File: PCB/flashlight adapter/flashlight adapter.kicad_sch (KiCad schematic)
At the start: 26 parts, among them J1 USB4105-GF-A, Q1 Q_NMOS_Depletion, Q2 Q_NMOS_Depletion, U1 MIC2295YD5-TR, U3 BQ24074RGT, U4 DW01A

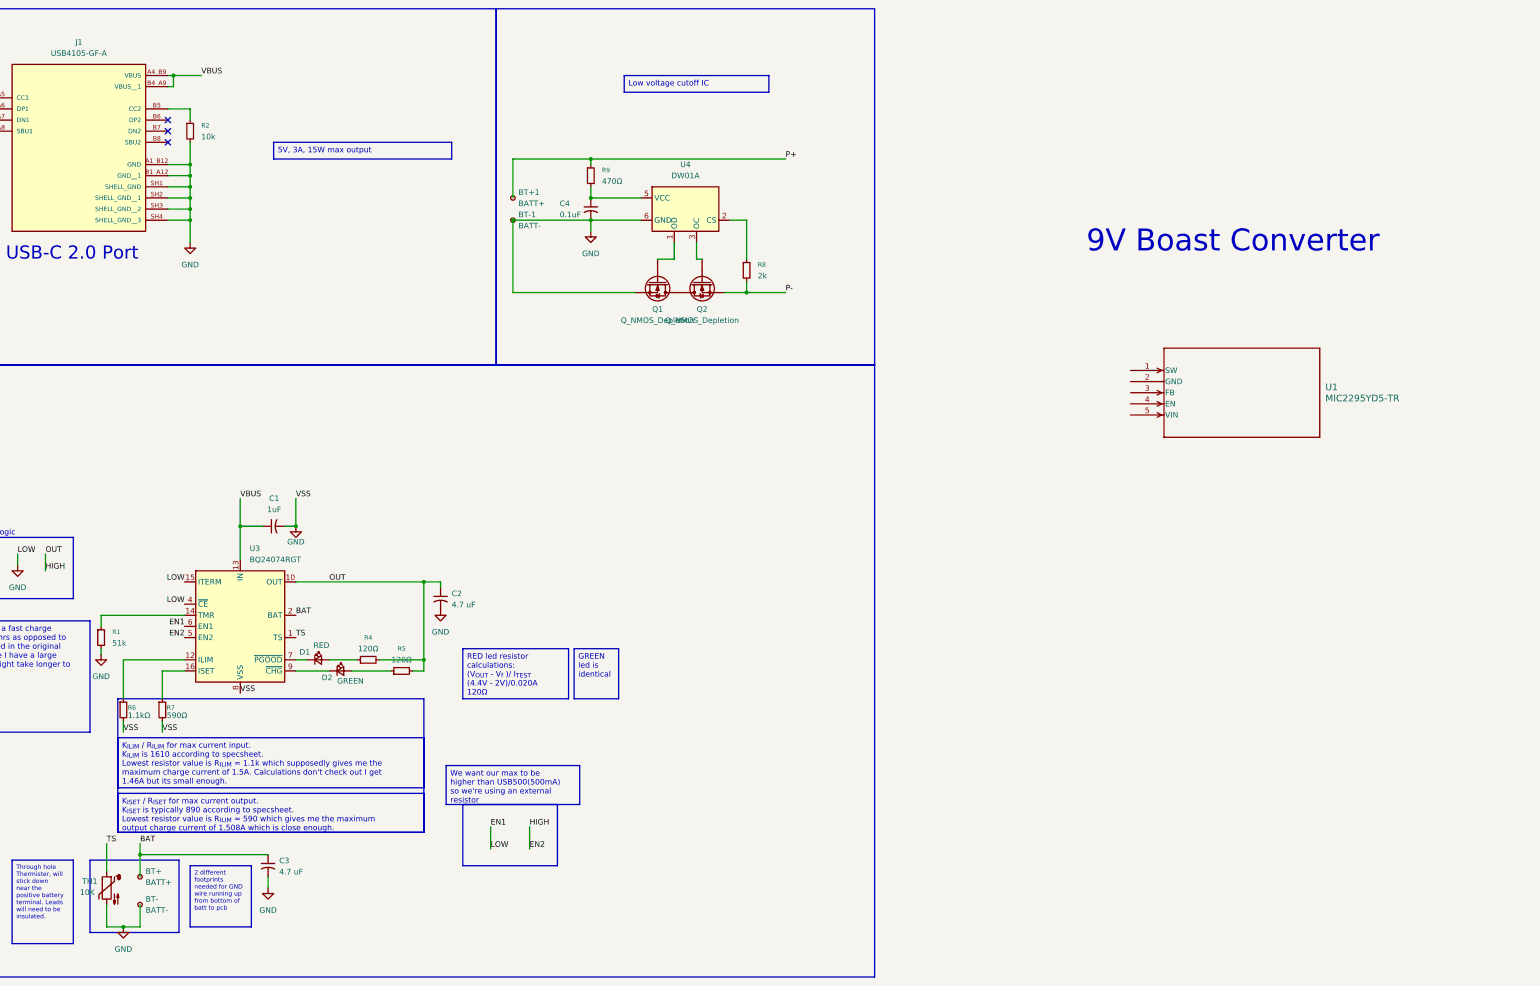
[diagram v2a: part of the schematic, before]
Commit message: almost completed boast converter, waiting on inductor resistor feedback
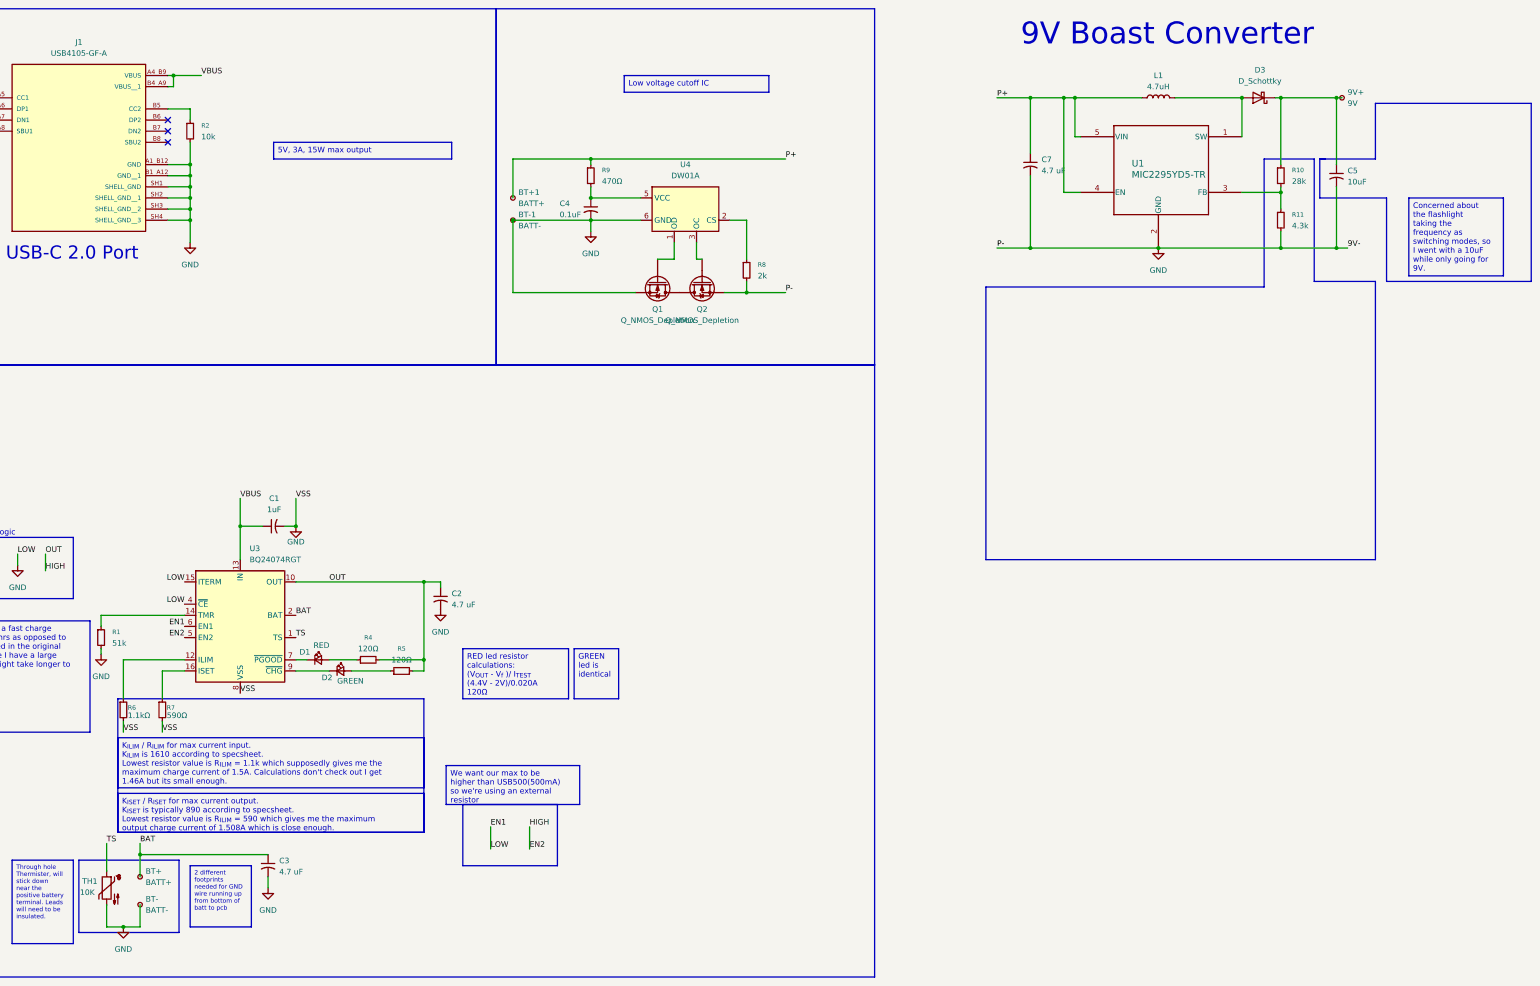
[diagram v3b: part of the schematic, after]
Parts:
- added 9V+: 9V, symbol Connector:TestPoint_Small
- added C5: 10uF, Capacitor_SMD:C_0805_2012Metric_Pad1.18x1.45mm_HandSolder, symbol Device:C_Small_US
- added C7: 4.7 uF, Capacitor_SMD:C_0603_1608Metric_Pad1.08x0.95mm_HandSolder, symbol Device:C_Small_US
- added D3: D_Schottky, Diode_SMD:D_SMA_Handsoldering, symbol Device:D_Schottky
- added L1: 4.7uH, Inductor_SMD:L_1008_2520Metric_Pad1.43x2.20mm_HandSolder, symbol Device:L
- added R10: 28k, Resistor_SMD:R_0603_1608Metric_Pad0.98x0.95mm_HandSolder, symbol Device:R_Small
- added R11: 4.3k, Resistor_SMD:R_0603_1608Metric_Pad0.98x0.95mm_HandSolder, symbol Device:R_Small
- U1: footprint Package_TO_SOT_SMD:TSOT-23-5_HandSoldering -> TSOT-23-5_D5_MCH
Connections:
- net P- is gone; now on net GND: Q2.S, R8.2
- net GND: now also U1.2 (GND), C5.2, C7.2, R11.2
- net P+: now also U1.4 (EN), U1.5 (VIN), C7.1, L1.1
- net at U1.1 (SW): now also D3.2 (A), L1.2
- net at U1.3 (FB): now also R10.2, R11.1
- new net: 9V+.1, C5.1, D3.1 (K), R10.1

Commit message: Pretty much finished schematic
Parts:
- removed BT+1: BATT+, symbol Connector:TestPoint_Small
- removed BT-1: BATT-, symbol Connector:TestPoint_Small
- 9V+1: renamed from 9V+; footprint (none) -> pads:4mm_by_4mm_pad
- BT+1: renamed from BT+; footprint (none) -> pads:4mm_by_4mm_pad
- BT-1: renamed from BT-; footprint (none) -> pads:3mm_by_4mm_pad
- J1: footprint USB4105-GF-A:GCT_USB4105-GF-A -> USB4105_GF_A:GCT_USB4105-GF-A
- Q1: footprint (none) -> DN2625K4:TO-252-3_MCH-L; symbol Device:Q_NMOS_Depletion -> Transistor_FET_Other:Q_NMOS_Depletion_GSD
- Q2: value Q_NMOS_Depletion -> Q_NMOS_Depletion_GSD; footprint (none) -> DN2625K4:TO-252-3_MCH-L; symbol Device:Q_NMOS_Depletion -> Transistor_FET_Other:Q_NMOS_Depletion_GSD
- U3: renamed from U1; footprint TSOT-23-5_D5_MCH -> Package_TO_SOT_SMD:TSOT-23-5_HandSoldering
- renumbered C3 to C1, C1 to C2, C2 to C3, C7 to C5, C5 to C6, R3 to R1, R1 to R2, R6 to R3, R7 to R4, R2 to R5, R4 to R6, R5 to R7, R9 to R8, R8 to R9, U3 to U1, U4 to U2
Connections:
- net P+ is gone; now on net BAT: C5.1, L1.1, R8.1, U3.4 (EN), U3.5 (VIN)
- net GND: now also Q1.2 (S), Q2.2 (S); no longer Q1.S, Q2.S
- net at U2.1 (OD): now also Q1.1 (G); no longer Q1.G
- net at U2.3 (OC): now also Q2.1 (G); no longer Q2.G
- new net: Q1.3 (D), Q2.3 (D)

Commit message: Intial layout complete with DRC, test pads to be added
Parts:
- removed Q1: Q_NMOS_Depletion, DN2625K4:TO-252-3_MCH-L, symbol Transistor_FET_Other:Q_NMOS_Depletion_GSD
- removed Q2: Q_NMOS_Depletion_GSD, DN2625K4:TO-252-3_MCH-L, symbol Transistor_FET_Other:Q_NMOS_Depletion_GSD
- added Q1: FS8205A, FS8205A:SOP65P640X120-8N, symbol FS8205A:FS8205A
- D3: footprint Diode_SMD:D_SMA_Handsoldering -> Diode_SMD:D_SOD-123F
- R9: value 2k -> 2kΩ
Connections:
- net GND: now also Q1.2, Q1.3; no longer C5.2, C6.2, R11.2, R9.2, U3.2 (GND)
- net at U2.1 (OD): now also Q1.4
- net at U2.3 (OC): now also Q1.5
- new net: Q1.1, Q1.8
- new net P-: C5.2, C6.2, Q1.6, Q1.7, R11.2, R9.2, U3.2 (GND)
- no-connect marks 6 -> 7

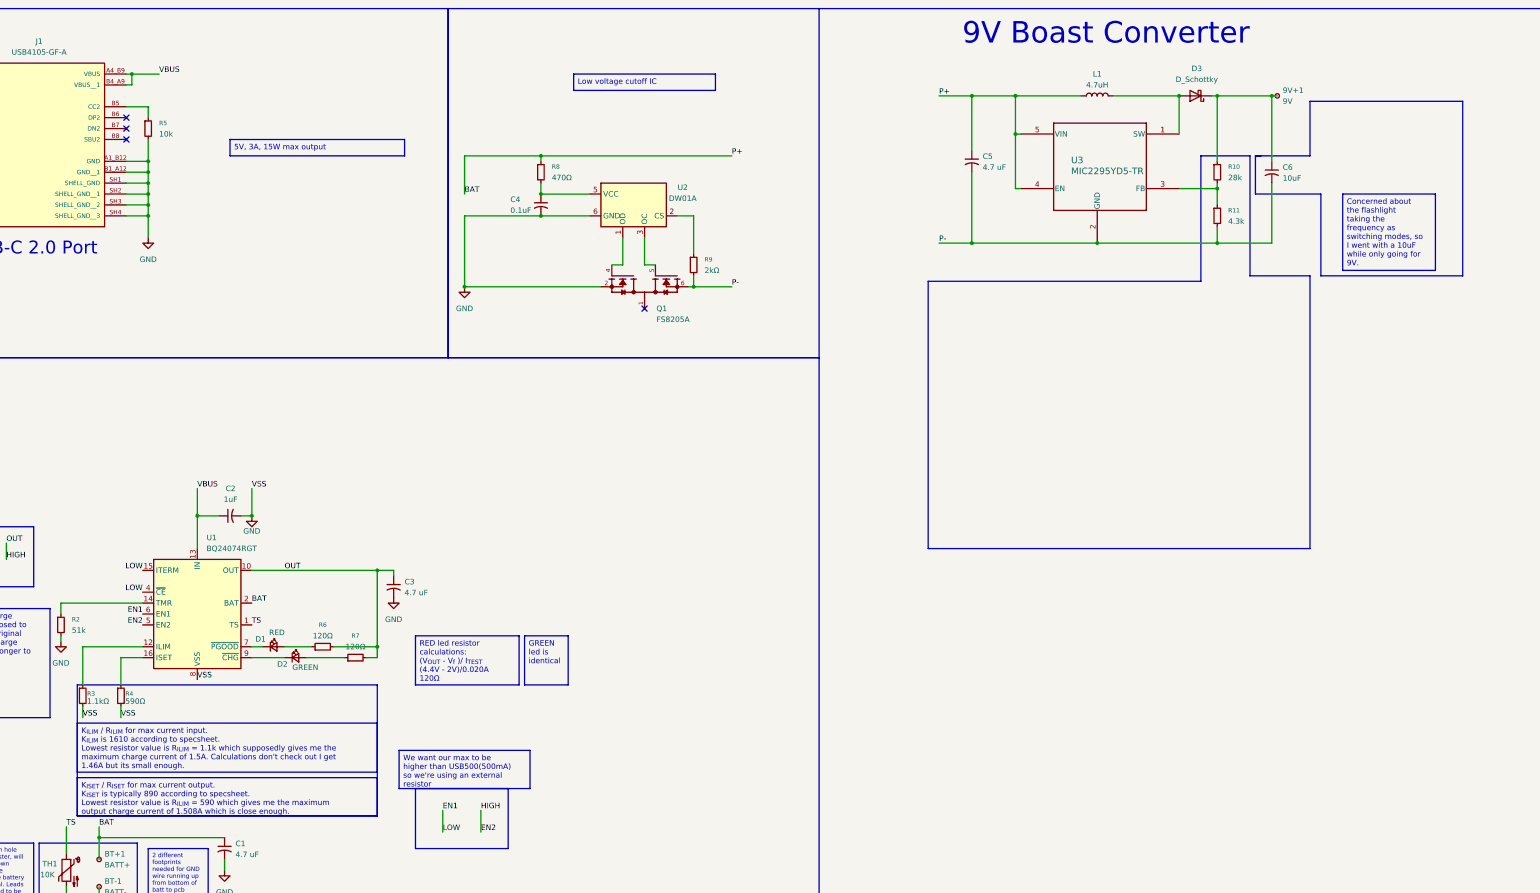
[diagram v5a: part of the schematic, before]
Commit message: Added Boost off when charging
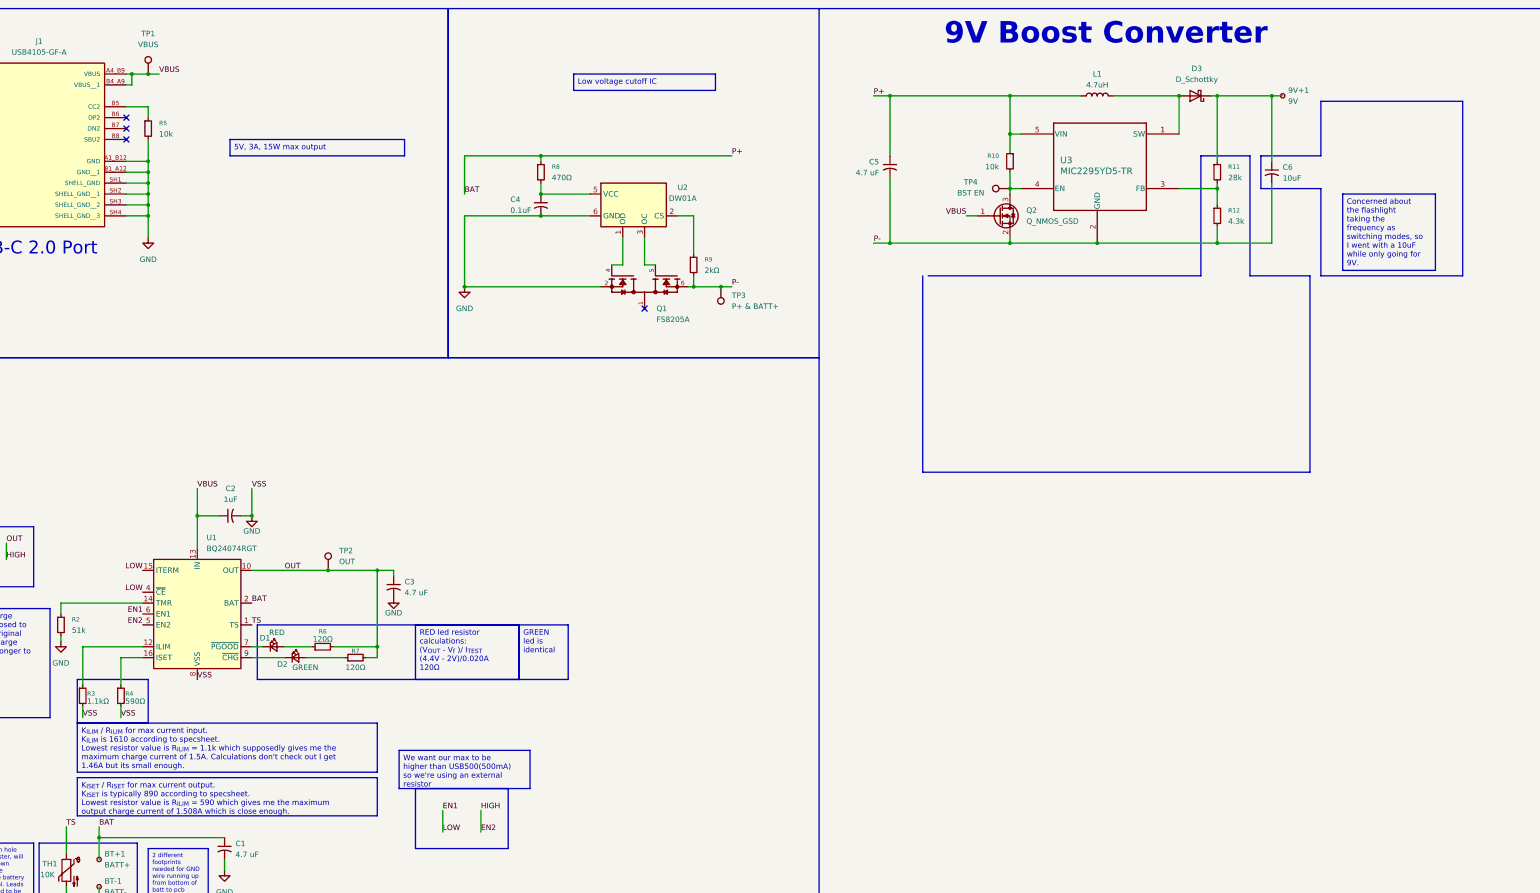
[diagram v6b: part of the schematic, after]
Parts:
- added Q2: Q_NMOS_GSD, Package_TO_SOT_SMD:SOT-23_Handsoldering, symbol Transistor_FET:Q_NMOS_GSD
- added R10: 10k, Resistor_SMD:R_0603_1608Metric_Pad0.98x0.95mm_HandSolder, symbol Device:R_Small
- added TP1: VBUS, TestPoint:TestPoint_Pad_D1.5mm, symbol Connector:TestPoint
- added TP2: OUT, TestPoint:TestPoint_Pad_D1.5mm, symbol Connector:TestPoint
- added TP3: P+ & BATT+, TestPoint:TestPoint_Pad_D1.5mm, symbol Connector:TestPoint
- added TP4: BST EN, TestPoint:TestPoint_Pad_D1.5mm, symbol Connector:TestPoint
- Q1: footprint FS8205A:SOP65P640X120-8N -> Package_TO_SOT_SMD:SOT-23-6_Handsoldering
- renumbered R10 to R11, R11 to R12
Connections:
- net BAT: now also R10.1; no longer U3.4 (EN)
- net EN2: now also TP2.1
- net P-: now also Q2.2 (S), TP3.1
- net VBUS: now also Q2.1 (G), TP1.1
- new net: Q2.3 (D), R10.2, TP4.1, U3.4 (EN)
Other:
- note added: "9V Boost Converter"
- note removed: "9V Boast Converter"
- moved on the sheet: 9V+1, C5

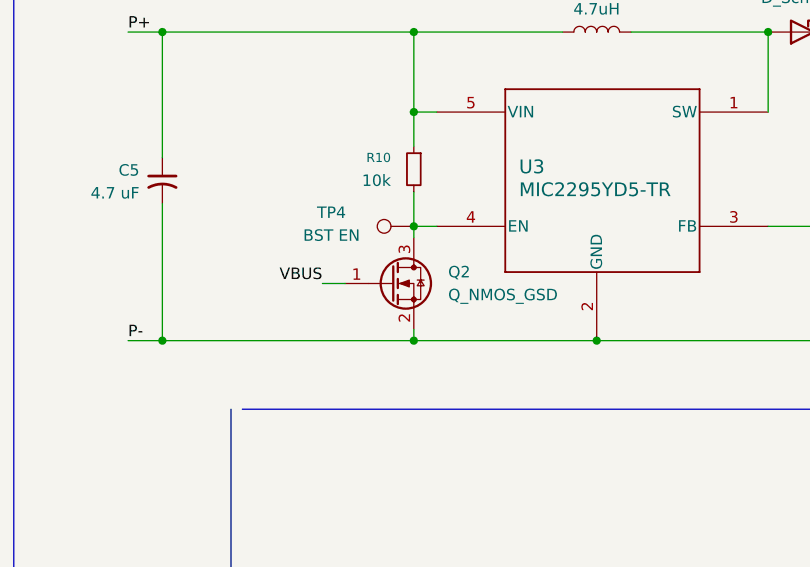
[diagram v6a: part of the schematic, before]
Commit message: Fixed usb switch mosfet footprint, sent out second order
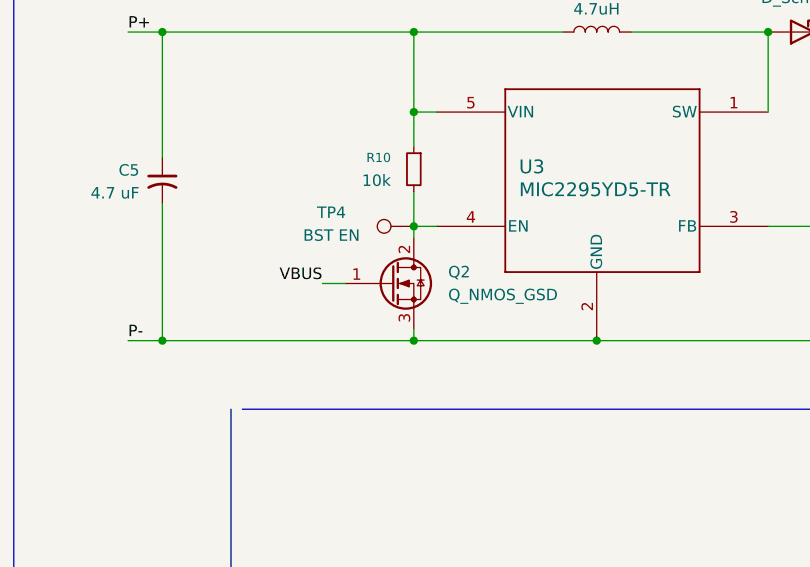
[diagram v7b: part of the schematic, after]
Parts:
- Q2: symbol Transistor_FET:Q_NMOS_GSD -> Transistor_FET:Q_NMOS_GDS
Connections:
- net P-: now also Q2.3 (S); no longer Q2.2 (S)
- net at R10.2, TP4.1, U3.4 (EN): now also Q2.2 (D); no longer Q2.3 (D)
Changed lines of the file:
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@@
 	)
 	(symbol
-		(lib_id "Transistor_FET:Q_NMOS_GSD")
+		(lib_id "Transistor_FET:Q_NMOS_GDS")
 		(at 274.32 109.22 0)
 		(unit 1)
@@
 			)
 		)
-		(property "Datasheet" "https://www.digikey.com/en/products/detail/diodes-incorporated/BSS138K-7-W/27803573"
+		(property "Datasheet" "~"
 			(at 274.32 109.22 0)
 			(effects
@@
 			)
 		)
-		(property "Description" "N-MOSFET transistor, gate/source/drain"
+		(property "Description" "N-MOSFET transistor, gate/drain/source"
 			(at 274.32 109.22 0)
 			(effects
